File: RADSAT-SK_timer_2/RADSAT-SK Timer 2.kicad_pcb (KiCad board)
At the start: 2 copper layers, 90.2 x 95.9 mm, 39 parts, among them J101 Conn_02x26_Odd_Even, J103 Conn_02x26_Odd_Even, J201 Conn_01x07, J202 Conn_01x04_Female, J203 Conn_01x03, J204 Conn_01x02, J205 Conn_01x02, J206 Conn_01x02, Q204 IRLML2060, Q205 IRLML2060, Q206 IRLML2060, SW201 SW_Push, SW202 SW_Push, SW203 SW_Push, SW204 SW_Push, SW205 SW_Push, SW206 SW_Push, U230 CPC1114N, U240 CPC1114N, U250 CPC1114N, U260 CPC1114N

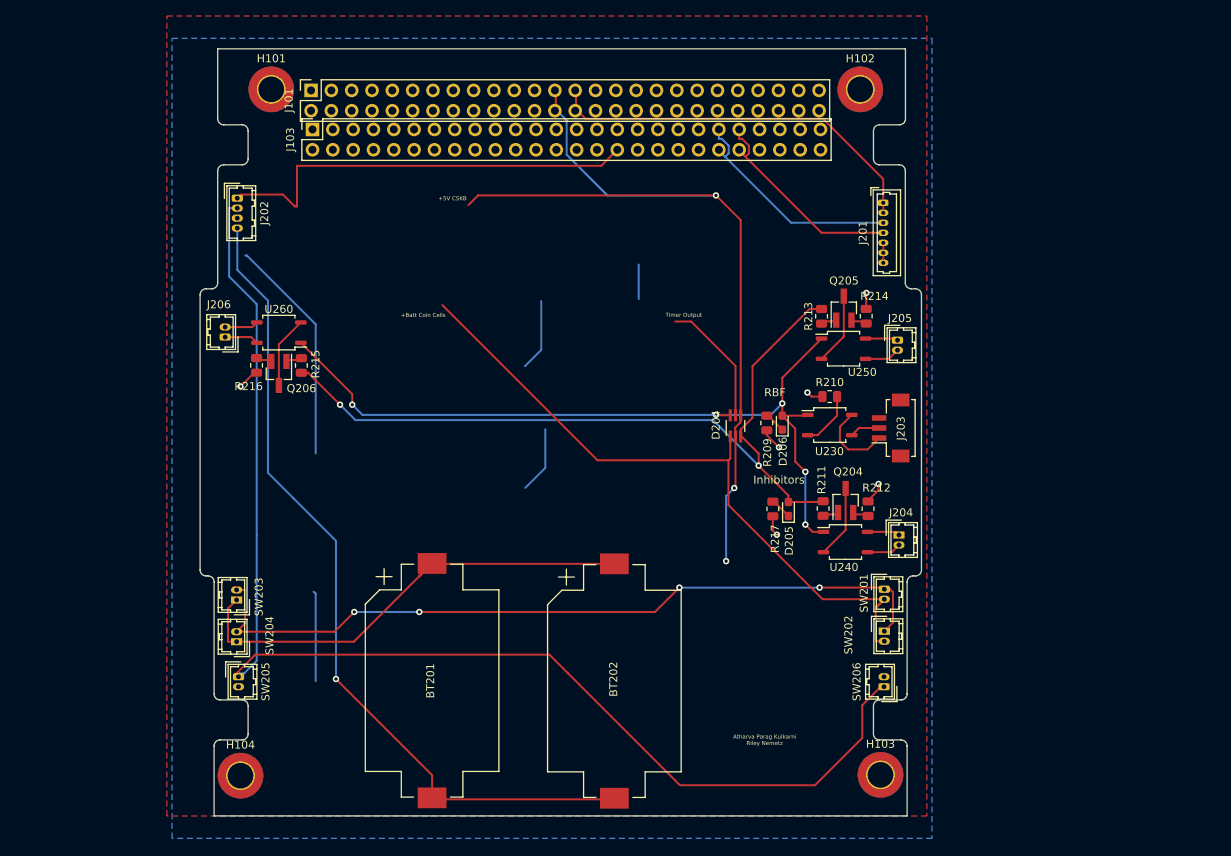
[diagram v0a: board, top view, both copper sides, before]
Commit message: added resistors in schematic, changed Voltage regulator
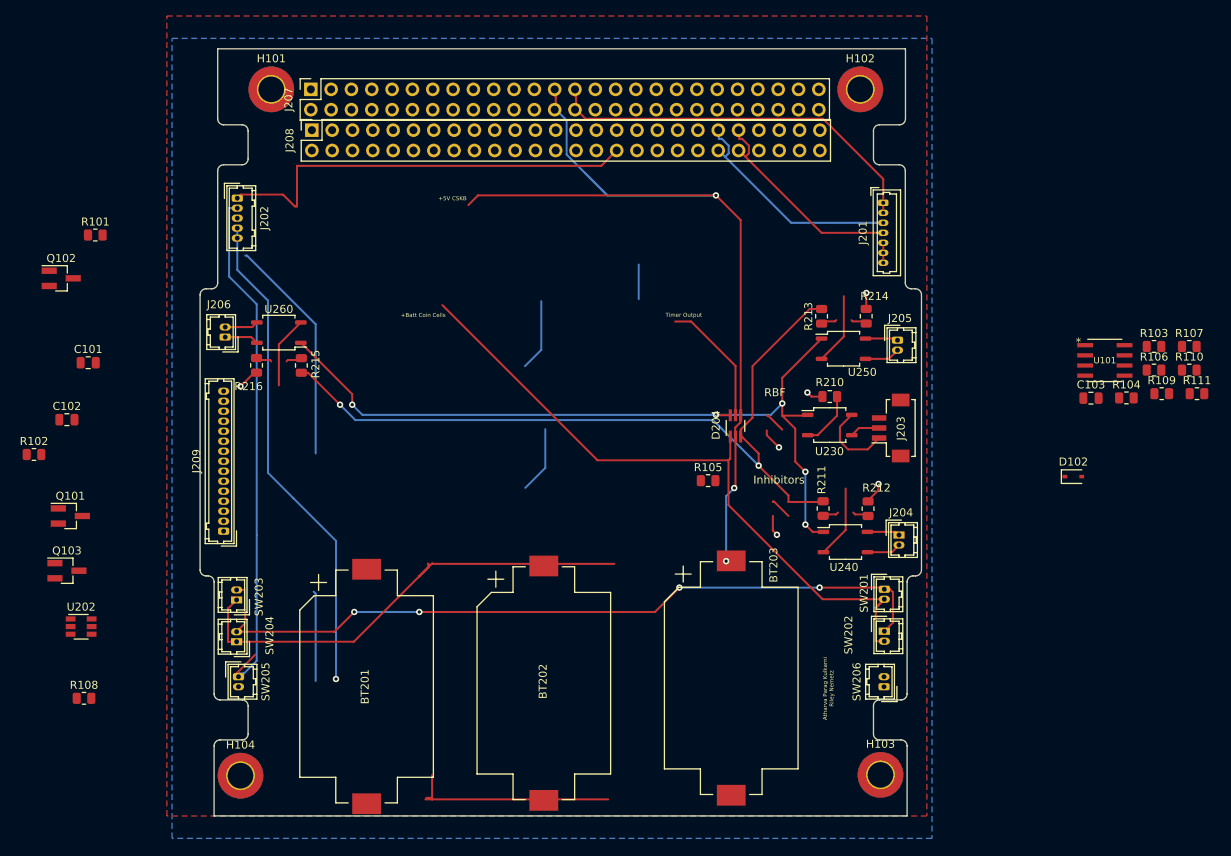
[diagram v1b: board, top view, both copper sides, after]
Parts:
- removed D205, D206: LED, LED_SMD:LED_0603_1608Metric_Pad1.05x0.95mm_HandSolder
- removed J101, J103: Conn_02x26_Odd_Even, Connector_PinSocket_2.54mm:PinSocket_2x26_P2.54mm_Vertical
- removed Q204, Q205, Q206: IRLML2060, Package_TO_SOT_SMD:SOT-23_Handsoldering
- removed R209, R217: 1k, Resistor_SMD:R_0805_2012Metric
- added BT203: Battery_Cell, Battery:BatteryHolder_Keystone_1060_1x2032, F.Cu at (101.2, 128.7)
- added C101: 0.1uF, Capacitor_SMD:C_0805_2012Metric, F.Cu at (20.8, 89.2)
- added C102: 1uF, Capacitor_SMD:C_0805_2012Metric, F.Cu at (18.2, 96.4)
- added C103: C, Capacitor_SMD:C_0805_2012Metric, F.Cu at (146.2, 93.7)
- added D102: RB751V40T1G, Diode_SMD:D_SOD-323, F.Cu at (144.0, 103.5)
- added J207: Conn_02x26_Odd_Even, Connector_PinSocket_2.54mm:PinSocket_2x26_P2.54mm_Vertical, F.Cu at (48.7, 55.1)
- added J208: Conn_02x26_Odd_Even, Connector_PinSocket_2.54mm:PinSocket_2x26_P2.54mm_Vertical, F.Cu at (48.8, 60.2)
- added J209: Conn_01x15, Connector_Hirose:Hirose_DF13-15P-1.25DSA_1x15_P1.25mm_Vertical, F.Cu at (37.8, 110.3)
- added Q101: IRLML2060, Package_TO_SOT_SMD:SOT-23_Handsoldering, F.Cu at (18.6, 108.4)
- added Q102: IRLML2060, Package_TO_SOT_SMD:SOT-23_Handsoldering, F.Cu at (17.5, 78.7)
- added Q103: IRLML2060, Package_TO_SOT_SMD:SOT-23_Handsoldering, F.Cu at (18.2, 115.2)
- added R101: 10k, Resistor_SMD:R_0805_2012Metric, F.Cu at (21.7, 73.3)
- added R102: 604K, Resistor_SMD:R_0805_2012Metric, F.Cu at (14.1, 100.7)
- added R103: R, Resistor_SMD:R_0805_2012Metric, F.Cu at (154.1, 87.2)
- added R104: R, Resistor_SMD:R_0805_2012Metric, F.Cu at (150.6, 93.6)
- added R105: 49.9k, Resistor_SMD:R_0805_2012Metric, F.Cu at (98.3, 104.0)
- added R106: 1M, Resistor_SMD:R_0805_2012Metric, F.Cu at (154.1, 90.2)
- added R107: 81, Resistor_SMD:R_0805_2012Metric, F.Cu at (158.5, 87.2)
- added R108: 100k, Resistor_SMD:R_0805_2012Metric, F.Cu at (20.3, 131.2)
- added R109: 1M, Resistor_SMD:R_0805_2012Metric, F.Cu at (155.0, 93.1)
- added R110: 60, Resistor_SMD:R_0805_2012Metric, F.Cu at (158.5, 90.2)
- added R111: 17, Resistor_SMD:R_0805_2012Metric, F.Cu at (159.4, 93.1)
- added U101: LT1521IS8-5TR, LT1521IS8-5TR:SO-8_S, F.Cu at (147.9, 89.0)
- added U202: TPS3700DDCR, Package_TO_SOT_SMD:TSOT-23-6, F.Cu at (20.0, 122.2)
- J202: value Conn_01x04_Female -> Conn_01x05_Female; footprint Connector_Hirose:Hirose_DF13-04P-1.25DSA_1x04_P1.25mm_Vertical -> Connector_Hirose:Hirose_DF13-05P-1.25DSA_1x05_P1.25mm_Vertical
- R210: value 1k -> 320
- R211, R213, R215: value 100 -> 25
- R212, R214, R216: value 1k -> 80
- moved BT202 8.82 mm to (77.8, 129.3)
- moved BT201 8.22 mm to (55.6, 129.7)
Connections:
- net +3V3 renamed Test_CSKB_3V3
- net +BATT renamed B
- net /RADSAT-SK Timer 2/Inhib_in renamed Test_Relay_Inhibs
- net Net-(BT201-Pad1) renamed A
- net Net-(SW201-Pad1) renamed Test_SW1
- BT201 pad 2: Net-(BT201-Pad2) -> Test_negetive_Batt
- BT202 pad 2: Net-(BT201-Pad2) -> Test_negetive_Batt
- D204 pad 2: +5V -> Net-(D204-Pad2)
- D204 pad 4: +5V -> Test_CSKB_5V
- D204 pad 6: InhibV+ -> Net-(D204-Pad6)
- J201 pad 5: GND -> Test_GND
- J201 pad 6: GND -> Test_GND
- J201 pad 7: GND -> Test_GND
- J202 pad 1: USB_Charge -> Test_USB_Charge
- J202 pad 2: Net-(J202-Pad2) -> Net-(D204-Pad6)
- J202 pad 3: GND -> Net-(J202-Pad3)
- J202 pad 4: Net-(BT201-Pad2) -> InhibV+
- R210 pad 2: GND -> Test_GND
- R212 pad 2: GND -> Test_GND
- R214 pad 2: GND -> Test_GND
- R216 pad 2: GND -> Test_GND
- SW205 pad 1: Net-(J202-Pad2) -> Net-(J202-Pad3)
- SW205 pad 2: GND -> Test_GND
- SW206 pad 1: Net-(J202-Pad2) -> Net-(J202-Pad3)
- SW206 pad 2: GND -> Test_GND
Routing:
- net Test_CSKB_5V: track 0.00 -> 114.9 mm, vias 0 -> 3
- net +5V: track 114.9 -> 0.00 mm, vias 3 -> 0
- net Net-(J202-Pad2): track 159.8 -> 67.0 mm
- net GND: track 79.0 -> 0.00 mm, vias 6 -> 0
- net Test_GND: track 0.00 -> 79.0 mm, vias 0 -> 6
- net USB_Charge: track 54.2 -> 0.00 mm
- net Test_USB_Charge: track 0.00 -> 54.2 mm
- net Net-(BT201-Pad2): track 106.0 -> 61.5 mm
- net Test_negetive_Batt: track 0.00 -> 27.5 mm
- added copper zone on F.Cu, net +BATT
- added copper zone on B.Cu, net Test_GND
- removed copper zone on F.Cu, net B
- removed copper zone on B.Cu, net GND

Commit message: routed PCB
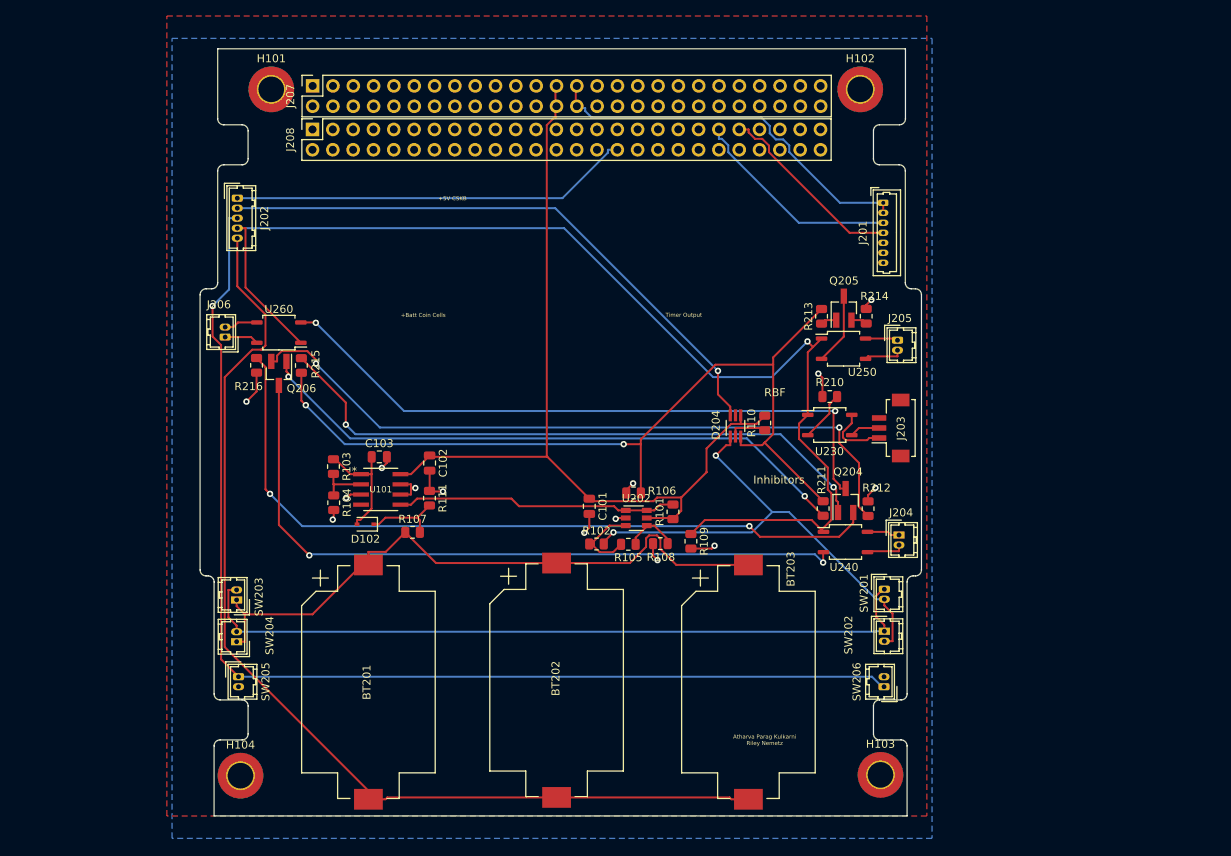
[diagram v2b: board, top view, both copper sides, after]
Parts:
- removed J209: Conn_01x15, Connector_Hirose:Hirose_DF13-15P-1.25DSA_1x15_P1.25mm_Vertical
- removed Q101, Q102, Q103: IRLML2060, Package_TO_SOT_SMD:SOT-23_Handsoldering
- added Q204: IRLML2060, Package_TO_SOT_SMD:SOT-23_Handsoldering, F.Cu at (115.5, 106.5)
- added Q205: IRLML2060, Package_TO_SOT_SMD:SOT-23_Handsoldering, F.Cu at (115.3, 82.4)
- added Q206: IRLML2060, Package_TO_SOT_SMD:SOT-23_Handsoldering, F.Cu at (44.7, 90.6)
- moved R103 103.7 mm to (51.5, 102.2), turned to 270 degrees
- moved R104 100.0 mm to (51.5, 106.7), turned to 270 degrees
- moved R107 99.8 mm to (61.4, 110.4)
- moved R111 96.8 mm to (63.5, 106.2), turned to 270 degrees
- moved U101 91.9 mm to (57.4, 105.1)
- moved C103 89.3 mm to (57.2, 101.0)
- moved D102 88.7 mm to (55.5, 109.4), turned to 180 degrees
- moved R101 80.1 mm to (93.9, 107.9), turned to 90 degrees
- moved R108 74.6 mm to (92.4, 111.8)
- moved R102 71.2 mm to (84.4, 111.9)
- moved U202 70.7 mm to (89.3, 108.7)
- moved R106 66.8 mm to (89.0, 105.5), turned to 180 degrees
- moved C101 65.2 mm to (83.5, 107.2), turned to 270 degrees
- moved R109 61.7 mm to (96.2, 111.6), turned to 270 degrees
- moved R110 53.5 mm to (105.4, 96.8), turned to 90 degrees
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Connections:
- net Test_CSKB_3V3 renamed +3V3
- net Test_CSKB_5V renamed +5V
- net Test_GND renamed GND
- net Test_INA+ renamed Net-(R102-Pad1)
- net Test_INB- renamed Net-(R105-Pad1)
- net Test_Relay_Inhibs renamed /Inhib_in
- net Test_SW1 renamed Net-(SW201-Pad1)
- net Test_USB_Charge renamed USB_Charge
- net Test_Vreg renamed Net-(C103-Pad1)
- net Test_negetive_Batt renamed Net-(BT201-Pad2)
- D204 pad 5: Inhib_EN -> (no net)
- J203 pad 3: Net-(J203-Pad3) -> (no net)
- J207 pad 1: Net-(J207-Pad1) -> (no net)
- J207 pad 10: Net-(J207-Pad10) -> (no net)
- J207 pad 11: Net-(J207-Pad11) -> (no net)
- J207 pad 12: Net-(J207-Pad12) -> (no net)
- J207 pad 13: Net-(J207-Pad13) -> (no net)
- J207 pad 14: Net-(J207-Pad14) -> (no net)
- J207 pad 15: Net-(J207-Pad15) -> (no net)
- J207 pad 16: Net-(J207-Pad16) -> (no net)
- J207 pad 17: Net-(J207-Pad17) -> (no net)
- J207 pad 18: Net-(J207-Pad18) -> (no net)
- J207 pad 19: Net-(J207-Pad19) -> (no net)
- J207 pad 2: Net-(J207-Pad2) -> (no net)
- J207 pad 20: Net-(J207-Pad20) -> (no net)
- J207 pad 21: Net-(J207-Pad21) -> (no net)
- J207 pad 22: Net-(J207-Pad22) -> (no net)
- J207 pad 23: Net-(J207-Pad23) -> (no net)
- J207 pad 24: Net-(J207-Pad24) -> (no net)
- J207 pad 3: Net-(J207-Pad3) -> (no net)
- J207 pad 31: Net-(J207-Pad31) -> (no net)
- J207 pad 33: Net-(J207-Pad33) -> (no net)
- J207 pad 34: Net-(J207-Pad34) -> (no net)
- J207 pad 35: Net-(J207-Pad35) -> (no net)
- J207 pad 36: Net-(J207-Pad36) -> (no net)
- J207 pad 37: Net-(J207-Pad37) -> (no net)
- J207 pad 38: Net-(J207-Pad38) -> (no net)
- J207 pad 39: Net-(J207-Pad39) -> (no net)
- J207 pad 4: Net-(J207-Pad4) -> (no net)
- J207 pad 40: Net-(J207-Pad40) -> (no net)
- J207 pad 41: Net-(J207-Pad41) -> (no net)
- J207 pad 42: Net-(J207-Pad42) -> (no net)
- J207 pad 43: Net-(J207-Pad43) -> (no net)
- J207 pad 44: Net-(J207-Pad44) -> (no net)
- J207 pad 45: Net-(J207-Pad45) -> (no net)
- J207 pad 46: Net-(J207-Pad46) -> (no net)
- J207 pad 47: Net-(J207-Pad47) -> (no net)
- J207 pad 48: Net-(J207-Pad48) -> (no net)
- J207 pad 49: Net-(J207-Pad49) -> (no net)
- J207 pad 5: Net-(J207-Pad5) -> (no net)
- J207 pad 50: Net-(J207-Pad50) -> (no net)
- J207 pad 51: Net-(J207-Pad51) -> (no net)
- J207 pad 52: Net-(J207-Pad52) -> (no net)
- J207 pad 6: Net-(J207-Pad6) -> (no net)
- J207 pad 7: Net-(J207-Pad7) -> (no net)
- J207 pad 8: Net-(J207-Pad8) -> (no net)
- J207 pad 9: Net-(J207-Pad9) -> (no net)
- J208 pad 1: Net-(J208-Pad1) -> (no net)
- J208 pad 10: Net-(J208-Pad10) -> (no net)
- J208 pad 11: Net-(J208-Pad11) -> (no net)
- J208 pad 12: Net-(J208-Pad12) -> (no net)
- J208 pad 13: Net-(J208-Pad13) -> (no net)
- J208 pad 14: Net-(J208-Pad14) -> (no net)
- J208 pad 15: Net-(J208-Pad15) -> (no net)
- J208 pad 16: Net-(J208-Pad16) -> (no net)
- J208 pad 17: Net-(J208-Pad17) -> (no net)
- J208 pad 18: Net-(J208-Pad18) -> (no net)
- J208 pad 19: Net-(J208-Pad19) -> (no net)
- J208 pad 2: Net-(J208-Pad2) -> (no net)
- J208 pad 20: Net-(J208-Pad20) -> (no net)
- J208 pad 21: Net-(J208-Pad21) -> (no net)
- J208 pad 22: Net-(J208-Pad22) -> (no net)
- J208 pad 23: Net-(J208-Pad23) -> (no net)
- J208 pad 24: Net-(J208-Pad24) -> (no net)
- J208 pad 25: Net-(J208-Pad25) -> (no net)
- J208 pad 26: Net-(J208-Pad26) -> (no net)
- J208 pad 27: Net-(J208-Pad27) -> (no net)
- J208 pad 28: Net-(J208-Pad28) -> (no net)
- J208 pad 29: Net-(J208-Pad29) -> (no net)
- J208 pad 3: Net-(J208-Pad3) -> (no net)
- J208 pad 30: Net-(J208-Pad30) -> (no net)
- J208 pad 31: Net-(J208-Pad31) -> (no net)
- J208 pad 33: Net-(J208-Pad33) -> (no net)
- J208 pad 34: Net-(J208-Pad34) -> (no net)
- J208 pad 35: Net-(J208-Pad35) -> (no net)
- J208 pad 36: Net-(J208-Pad36) -> (no net)
- J208 pad 37: Net-(J208-Pad37) -> (no net)
- J208 pad 38: Net-(J208-Pad38) -> (no net)
- J208 pad 39: Net-(J208-Pad39) -> (no net)
- J208 pad 4: Net-(J208-Pad4) -> (no net)
- J208 pad 40: Net-(J208-Pad40) -> (no net)
- J208 pad 42: Net-(J208-Pad42) -> (no net)
- J208 pad 44: Net-(J208-Pad44) -> (no net)
- J208 pad 45: Net-(J208-Pad45) -> (no net)
- J208 pad 46: Net-(J208-Pad46) -> (no net)
- J208 pad 47: Net-(J208-Pad47) -> (no net)
- J208 pad 48: Net-(J208-Pad48) -> (no net)
- J208 pad 49: Net-(J208-Pad49) -> (no net)
- J208 pad 5: Net-(J208-Pad5) -> (no net)
- J208 pad 50: Net-(J208-Pad50) -> (no net)
- J208 pad 51: Net-(J208-Pad51) -> (no net)
- J208 pad 52: Net-(J208-Pad52) -> (no net)
- J208 pad 6: Net-(J208-Pad6) -> (no net)
- J208 pad 7: Net-(J208-Pad7) -> (no net)
- J208 pad 8: Net-(J208-Pad8) -> (no net)
- J208 pad 9: Net-(J208-Pad9) -> (no net)
- U101 pad 4: Net-(U101-Pad4) -> (no net)
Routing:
- net Net-(J202-Pad3): track 0.00 -> 141.8 mm, vias 0 -> 1
- net Net-(BT201-Pad2): track 27.5 -> 129.9 mm
- net Net-(Q204-Pad2): track 2.45 -> 94.8 mm, vias 0 -> 2
- net Net-(Q206-Pad2): track 2.17 -> 88.7 mm, vias 0 -> 2
- net Net-(Q206-Pad3): track 9.10 -> 88.8 mm, vias 0 -> 2
- net Net-(Q204-Pad1): track 2.03 -> 78.2 mm, vias 0 -> 2
- net Net-(D204-Pad6): track 0.00 -> 74.7 mm, vias 0 -> 1
- net Net-(Q206-Pad1): track 2.03 -> 76.1 mm, vias 0 -> 2
- net Net-(Q204-Pad3): track 9.01 -> 82.2 mm, vias 0 -> 2
- net Net-(J202-Pad2): track 67.0 -> 0.00 mm
- net Net-(BT201-Pad2) (its old number): track 61.5 -> 0.00 mm, vias 1 -> 0
- net InhibV+: track 99.4 -> 145.2 mm, vias 5 -> 1
- net GND: track 79.0 -> 35.2 mm, vias 6 -> 14
- net CHRG_ON-OFF: track 0.00 -> 35.3 mm
- net B: track 85.4 -> 61.5 mm, vias 0 -> 2
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
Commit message: added test points
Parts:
- added TP101: TestPoint, S2761-46R:HARWIN_S2761-46R, F.Cu at (96.3, 100.4)
- added TP102: TestPoint, S2761-46R:HARWIN_S2761-46R, F.Cu at (100.1, 104.6)
- added TP103: TestPoint, S2761-46R:HARWIN_S2761-46R, F.Cu at (115.3, 118.7)
- added TP104: TestPoint, S2761-46R:HARWIN_S2761-46R, F.Cu at (89.0, 65.7)
- added TP105: TestPoint, S2761-46R:HARWIN_S2761-46R, F.Cu at (115.7, 62.7)
- added TP106: TestPoint, S2761-46R:HARWIN_S2761-46R, F.Cu at (80.1, 65.6)
- added TP107: TestPoint, S2761-46R:HARWIN_S2761-46R, F.Cu at (116.7, 76.8)
- added TP108: TestPoint, S2761-46R:HARWIN_S2761-46R, F.Cu at (112.8, 74.4)
- added TP109: TestPoint, S2761-46R:HARWIN_S2761-46R, F.Cu at (106.9, 85.6)
- added TP110: TestPoint, S2761-46R:HARWIN_S2761-46R, F.Cu at (117.0, 67.8)
- added TP111: TestPoint, S2761-46R:HARWIN_S2761-46R, F.Cu at (102.7, 93.2)
- added TP112: TestPoint, S2761-46R:HARWIN_S2761-46R, F.Cu at (80.5, 111.2)
- added TP113: TestPoint, S2761-46R:HARWIN_S2761-46R, F.Cu at (93.4, 116.4)
- added TP114: TestPoint, S2761-46R:HARWIN_S2761-46R, F.Cu at (97.2, 107.6)
- added TP115: TestPoint, S2761-46R:HARWIN_S2761-46R, F.Cu at (94.0, 103.3)
- added TP116: TestPoint, S2761-46R:HARWIN_S2761-46R, F.Cu at (108.9, 81.7)
- C103: value C -> 10uF
- R103: value R -> 1k
- R104: value R -> 2k
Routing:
- net I2C_DATA: track 26.6 -> 42.8 mm
- net CHRG_ON-OFF: track 35.3 -> 48.4 mm, vias 0 -> 2
- net +3V3: track 48.4 -> 57.5 mm
- net B: track 61.5 -> 68.4 mm, vias 2 -> 3
- net +5V: track 109.3 -> 115.6 mm
- net A: track 81.1 -> 87.3 mm
- net Net-(R105-Pad1): track 6.84 -> 12.9 mm
- net InhibV+: track 145.2 -> 150.9 mm, vias 1 -> 2
- net Net-(D204-Pad6): track 74.7 -> 79.9 mm, vias 1 -> 2
- net Net-(SW201-Pad1): track 93.9 -> 98.8 mm
- net I2C_CLK: track 24.1 -> 28.9 mm
- net USB_Charge: track 50.2 -> 54.8 mm
- net GND: track 35.2 -> 39.0 mm, vias 14 -> 15
- net /Inhib_in: track 109.5 -> 113.1 mm
- net Net-(R102-Pad1): track 10.1 -> 13.4 mm
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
